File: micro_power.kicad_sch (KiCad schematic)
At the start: 24 parts

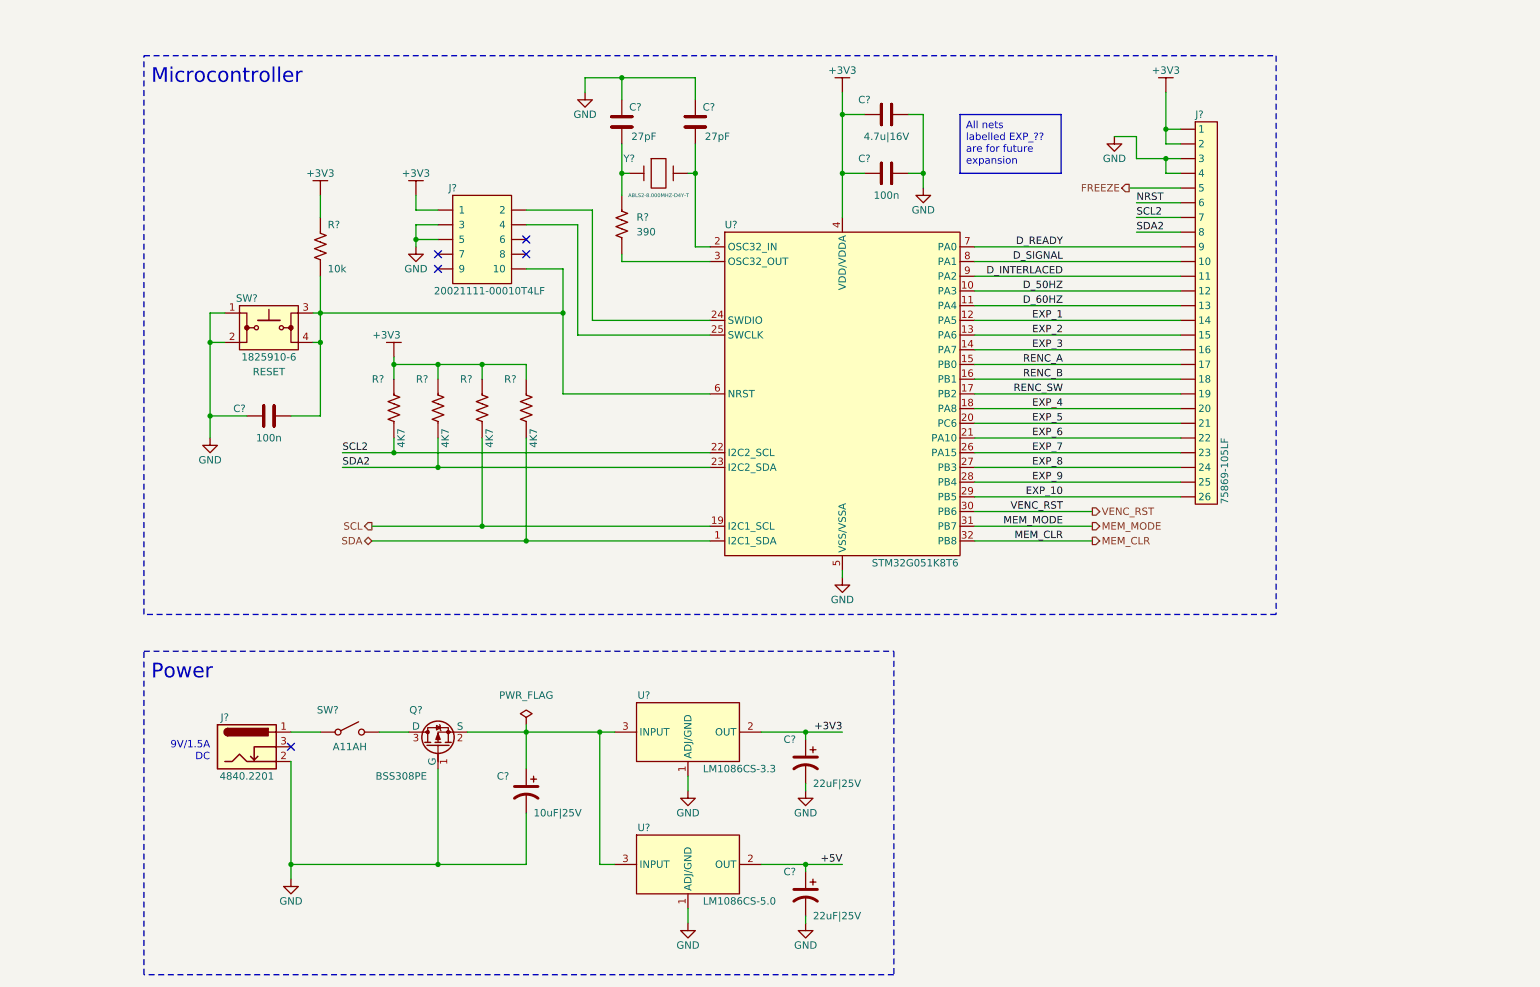
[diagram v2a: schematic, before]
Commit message: added connectors and crystal, osc
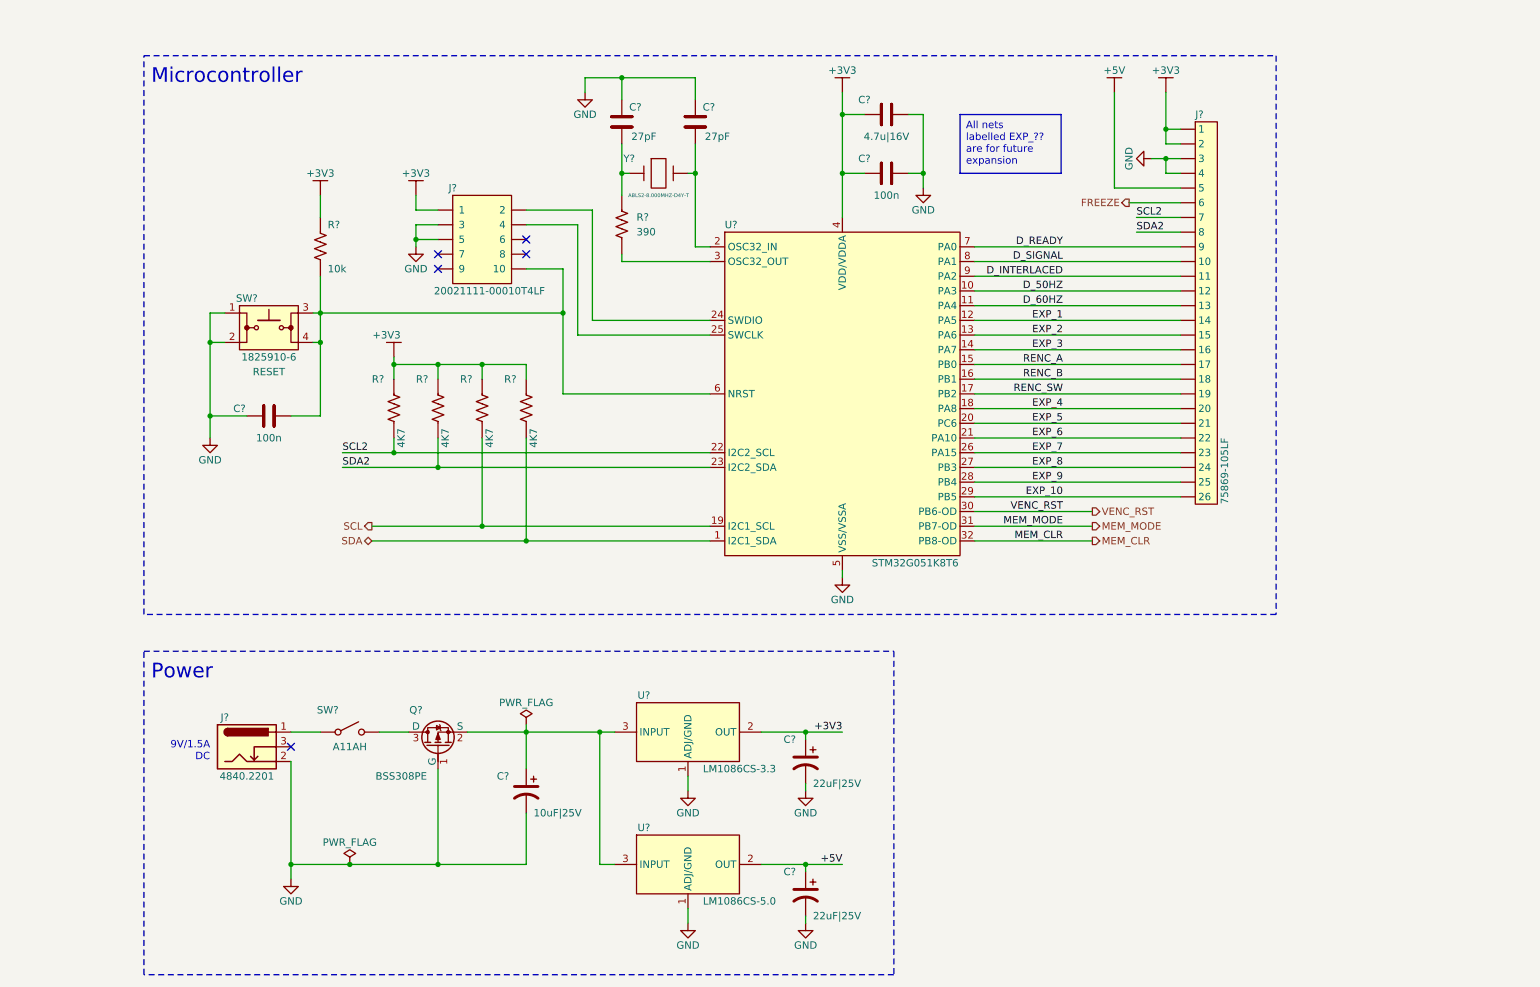
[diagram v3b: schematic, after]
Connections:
- net NRST is gone; now on net FREEZE: J?.6
- net +5V: now also J?.5
- net FREEZE: no longer J?.5
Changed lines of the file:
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@@
   (junction (at 83.82 76.2) (diameter 0) (color 0 0 0 0)
+  )
+  (junction (at 76.2 162.56) (diameter 0) (color 0 0 0 0)
   )
   (junction (at 106.68 106.68) (diameter 0) (color 0 0 0 0)
@@
     (stroke (width 0) (type default))
   )
+  (wire (pts (xy 76.2 162.56) (xy 91.44 162.56))
+    (stroke (width 0) (type default))
+  )
   (wire (pts (xy 184.15 106.68) (xy 204.47 106.68))
     (stroke (width 0) (type default))
@@
     (stroke (width 0) (type default))
   )
+  (wire (pts (xy 208.28 29.21) (xy 208.28 45.72))
+    (stroke (width 0) (type default))
+  )
   (wire (pts (xy 123.19 58.42) (xy 138.43 58.42))
     (stroke (width 0) (type default))
@@
     (stroke (width 0) (type default))
   )
-  (wire (pts (xy 212.09 40.64) (xy 217.17 40.64))
-    (stroke (width 0) (type default))
-  )
-  (wire (pts (xy 212.09 48.26) (xy 219.71 48.26))
+  (wire (pts (xy 214.63 40.64) (xy 217.17 40.64))
     (stroke (width 0) (type default))
   )
@@
     (stroke (width 0) (type default))
   )
-  (wire (pts (xy 66.04 162.56) (xy 91.44 162.56))
+  (wire (pts (xy 66.04 162.56) (xy 76.2 162.56))
     (stroke (width 0) (type default))
   )
@@
     (stroke (width 0) (type default))
   )
-  (wire (pts (xy 212.09 36.83) (xy 208.28 36.83))
-    (stroke (width 0) (type default))
-  )
   (wire (pts (xy 71.12 60.96) (xy 71.12 67.31))
     (stroke (width 0) (type default))
@@
     (stroke (width 0) (type default))
   )
-  (wire (pts (xy 212.09 36.83) (xy 212.09 40.64))
-    (stroke (width 0) (type default))
-  )
   (wire (pts (xy 106.68 153.67) (xy 106.68 162.56))
     (stroke (width 0) (type default))
@@
     (stroke (width 0) (type default))
   )
+  (wire (pts (xy 208.28 45.72) (xy 219.71 45.72))
+    (stroke (width 0) (type default))
+  )
   (wire (pts (xy 71.12 72.39) (xy 71.12 85.09))
     (stroke (width 0) (type default))
@@
     (stroke (width 0) (type default))
   )
-  (wire (pts (xy 210.82 45.72) (xy 219.71 45.72))
+  (wire (pts (xy 210.82 48.26) (xy 219.71 48.26))
     (stroke (width 0) (type default))
   )
@@
     (effects (font (size 1.27 1.27)) (justify right bottom))
   )
-  (label "NRST" (at 212.09 48.26 0) (fields_autoplaced)
-    (effects (font (size 1.27 1.27)) (justify left bottom))
-  )
   (label "EXP_1" (at 199.39 68.58 180) (fields_autoplaced)
     (effects (font (size 1.27 1.27)) (justify right bottom))
@@
     (effects (font (size 1.27 1.27)) (justify right))
   )
-  (hierarchical_label "FREEZE" (shape output) (at 210.82 45.72 180) (fields_autoplaced)
+  (hierarchical_label "FREEZE" (shape output) (at 210.82 48.26 180) (fields_autoplaced)
     (effects (font (size 1.27 1.27)) (justify right))
   )
@@
   )
   (symbol (lib_id "tbc:PWR_FLAG") (at 106.68 138.43 0) (unit 1)
-    (in_bom yes) (on_board yes) (dnp no) (fields_autoplaced)
+    (in_bom yes) (on_board yes) (dnp no)
     (property "Reference" "#FLG01" (at 106.68 136.525 0)
       (effects (font (size 1.27 1.27)) hide)
     )
-    (property "Value" "PWR_FLAG" (at 106.68 133.35 0)
+    (property "Value" "PWR_FLAG" (at 106.68 134.62 0)
       (effects (font (size 1.27 1.27)))
     )
@@
         (path "/9df71e53-7941-4fd3-a17d-93619e4e3e02/5f11175b-e91a-4557-963e-2b2820dad3c4"
           (reference "C?") (unit 1)
+        )
+      )
+    )
+  )
+  (symbol (lib_id "tbc:+5V") (at 208.28 29.21 0) (unit 1)
+    (in_bom yes) (on_board yes) (dnp no)
+    (property "Reference" "#PWR059" (at 208.28 39.37 0)
+      (effects (font (size 1.27 1.27)) hide)
+    )
+    (property "Value" "+5V" (at 208.28 25.4 0)
+      (effects (font (size 1.27 1.27)))
+    )
+    (property "Footprint" "" (at 208.28 29.21 0)
+      (effects (font (size 1.27 1.27)) hide)
+    )
+    (property "Datasheet" "" (at 208.28 29.21 0)
+      (effects (font (size 1.27 1.27)) hide)
+    )
+    (pin "1")
+    (instances
+      (project "tbc"
+        (path "/9df71e53-7941-4fd3-a17d-93619e4e3e02/5f11175b-e91a-4557-963e-2b2820dad3c4"
+          (reference "#PWR059") (unit 1)
         )
       )
@@
         (path "/9df71e53-7941-4fd3-a17d-93619e4e3e02/5f11175b-e91a-4557-963e-2b2820dad3c4"
           (reference "R?") (unit 1)
+        )
+      )
+    )
+  )
+  (symbol (lib_id "tbc:PWR_FLAG") (at 76.2 162.56 0) (unit 1)
+    (in_bom yes) (on_board yes) (dnp no)
+    (property "Reference" "#FLG02" (at 76.2 160.655 0)
+      (effects (font (size 1.27 1.27)) hide)
+    )
+    (property "Value" "PWR_FLAG" (at 76.2 158.75 0)
+      (effects (font (size 1.27 1.27)))
+    )
+    (property "Footprint" "" (at 76.2 162.56 0)
+      (effects (font (size 1.27 1.27)) hide)
+    )
+    (property "Datasheet" "~" (at 76.2 162.56 0)
+      (effects (font (size 1.27 1.27)) hide)
+    )
+    (pin "1")
+    (instances
+      (project "tbc"
+        (path "/9df71e53-7941-4fd3-a17d-93619e4e3e02/5f11175b-e91a-4557-963e-2b2820dad3c4"
+          (reference "#FLG02") (unit 1)
         )
       )
@@
     (pin "1" (alternate "I2C1_SDA"))
     (pin "18")
-    (pin "31")
+    (pin "31" (alternate "PB7-OD"))
     (pin "2" (alternate "OSC32_IN"))
     (pin "19" (alternate "I2C1_SCL"))
     (pin "23" (alternate "I2C2_SDA"))
-    (pin "30")
+    (pin "30" (alternate "PB6-OD"))
     (pin "17")
     (pin "22" (alternate "I2C2_SCL"))
     (pin "15")
-    (pin "32")
+    (pin "32" (alternate "PB8-OD"))
     (pin "7")
     (pin "9")
@@
     )
   )
-  (symbol (lib_id "tbc:GND") (at 208.28 36.83 0) (unit 1)
-    (in_bom yes) (on_board yes) (dnp no)
-    (property "Reference" "#PWR027" (at 208.28 43.18 0)
-      (effects (font (size 1.27 1.27)) hide)
-    )
-    (property "Value" "GND" (at 208.28 40.64 0)
-      (effects (font (size 1.27 1.27)))
-    )
-    (property "Footprint" "" (at 208.28 36.83 0)
-      (effects (font (size 1.27 1.27)) hide)
-    )
-    (property "Datasheet" "" (at 208.28 36.83 0)
-      (effects (font (size 1.27 1.27)) hide)
-    )
+  (symbol (lib_id "tbc:GND") (at 214.63 40.64 270) (unit 1)
+    (in_bom yes) (on_board yes) (dnp no)
+    (property "Reference" "#PWR027" (at 208.28 40.64 0)
+      (effects (font (size 1.27 1.27)) hide)
+    )
+    (property "Value" "GND" (at 210.82 40.64 0)
+      (effects (font (size 1.27 1.27)))
+    )
+    (property "Footprint" "" (at 214.63 40.64 0)
+      (effects (font (size 1.27 1.27)) hide)
+    )
+    (property "Datasheet" "" (at 214.63 40.64 0)
+      (effects (font (size 1.27 1.27)) hide)
+    )

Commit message: completed and annotated schematic, passed ERC
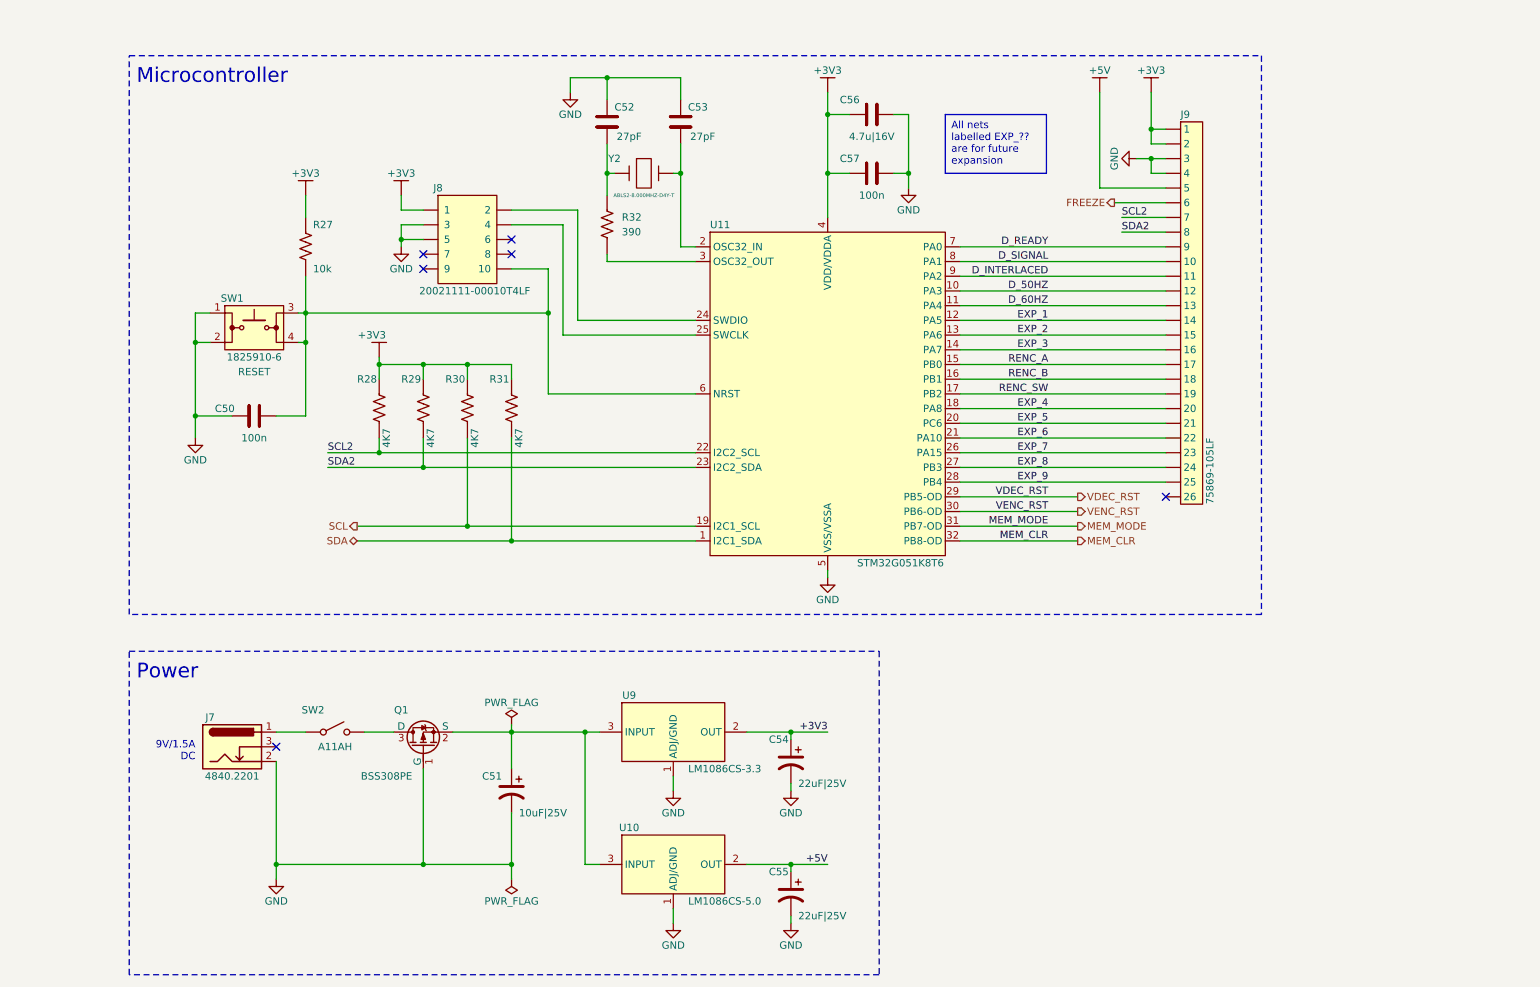
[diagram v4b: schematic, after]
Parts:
- gave numbers to parts that had none: 24
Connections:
- net EXP_10: no longer names the net of J9.26
- net EXP_10: no longer U11.29 (PB5)
- new net VDEC_RST: U11.29 (PB5)
- no-connect marks 5 -> 6
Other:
- moved on the sheet: C50, C51, C52, C53, C54, C55, C56, C57, J7, J8, J9, Q1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

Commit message: minor cleanup, addition of notes
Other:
- note added: "Note: P-MOSFET used for reverse polarity protection. High Vgs tolerance +/-20V eliminates need for zener and resistor in gate circuit."
- note added: "TODO: Check all GPIOs are capable of open drain configuration!"
- moved on the sheet: C51, C54, C55, J7, Q1, SW2, U10, U9

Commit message: added footprints for large ICs
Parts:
- U11: footprint (none) -> tbc:QFP32_7x7x1.6mm_Pitch0.8mm
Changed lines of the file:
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@@
       (effects (font (size 1.27 1.27)) (justify left))
     )
-    (property "Footprint" "" (at 158.75 44.45 0)
+    (property "Footprint" "tbc:QFP32_7x7x1.6mm_Pitch0.8mm" (at 158.75 44.45 0)
       (effects (font (size 1.27 1.27)) hide)
     )

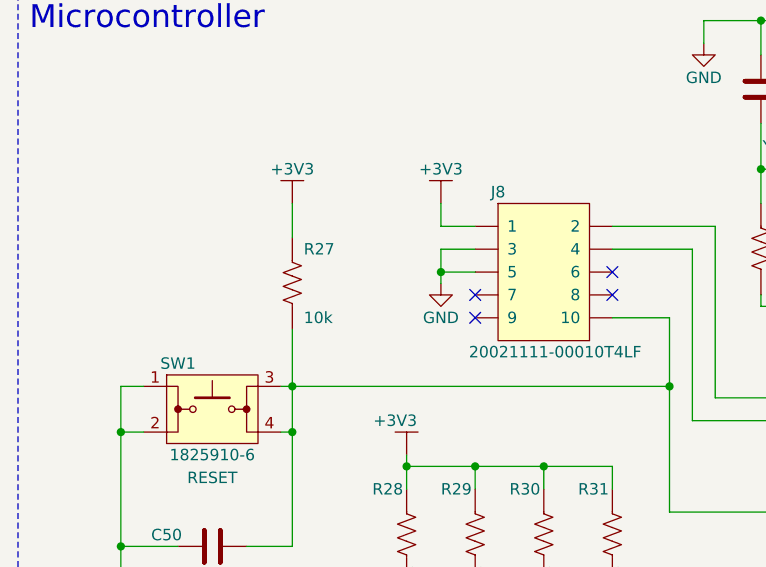
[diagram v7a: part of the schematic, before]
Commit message: resistor footprint added
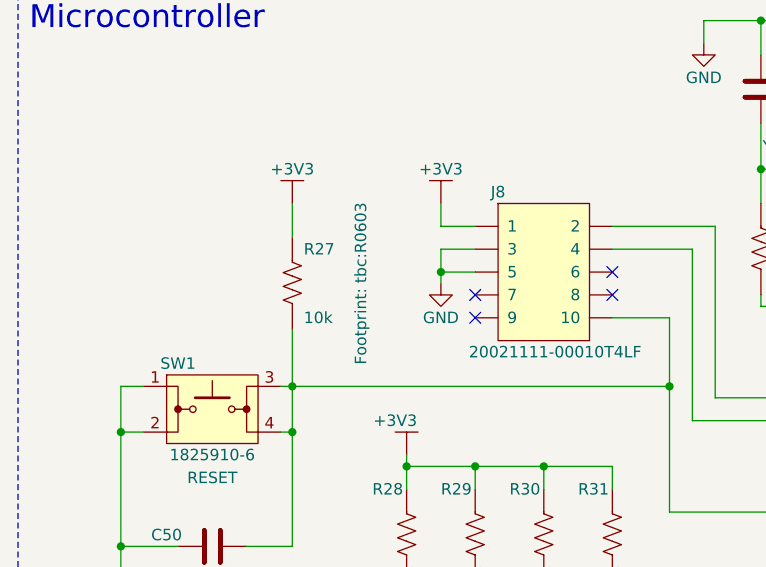
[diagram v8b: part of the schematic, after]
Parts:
- R27, R28, R29, R30, R31, R32: footprint (none) -> tbc:R0603
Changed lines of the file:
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@@
       (effects (font (size 1.27 1.27)))
     )
-    (property "Footprint" "" (at 88.9 100.33 0)
+    (property "Footprint" "tbc:R0603" (at 88.9 85.09 0) (show_name)
       (effects (font (size 1.27 1.27)) hide)
     )
@@
       (effects (font (size 1.27 1.27)))
     )
-    (property "Footprint" "" (at 96.52 100.33 0)
+    (property "Footprint" "tbc:R0603" (at 96.52 85.09 0) (show_name)
       (effects (font (size 1.27 1.27)) hide)
     )
@@
       (effects (font (size 1.27 1.27)))
     )
-    (property "Footprint" "" (at 104.14 100.33 0)
+    (property "Footprint" "tbc:R0603" (at 104.14 85.09 0) (show_name)
       (effects (font (size 1.27 1.27)) hide)
     )
@@
       (effects (font (size 1.27 1.27)) (justify right))
     )
-    (property "Footprint" "" (at 128.27 68.58 0)
+    (property "Footprint" "tbc:R0603" (at 128.27 52.07 0) (show_name)
       (effects (font (size 1.27 1.27)) hide)
     )
@@
       (effects (font (size 1.27 1.27)) (justify right))
     )
-    (property "Footprint" "" (at 76.2 72.39 0)
-      (effects (font (size 1.27 1.27)) hide)
+    (property "Footprint" "tbc:R0603" (at 76.2 55.88 0) (show_name)
+      (effects (font (size 1.27 1.27)))
     )
     (property "Datasheet" "https://www.mouser.com/datasheet/2/447/YAGEO_PYu_RC_Group_51_RoHS_L_12-3313492.pdf" (at 81.28 72.39 0) (show_name)
@@
       (effects (font (size 1.27 1.27)))
     )
-    (property "Footprint" "" (at 111.76 100.33 0)
-      (effects (font (size 1.27 1.27)) hide)
-    )
+    (property "Footprint" "tbc:R0603" (at 111.76 85.09 0) (show_name)
+      (effects (font (size 1.27 1.27)) hide)
+    )
